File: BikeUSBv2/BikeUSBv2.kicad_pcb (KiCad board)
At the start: 2 copper layers, 43.6 x 25.2 mm, 48 parts, among them J1 TYPE-C-31-M-16, J2 Conn_01x02_Female, Q1 SSM3J332R,LF, Q2 SSM3J332R,LF, SW1 SW_Push, SW2 SW_Push, U1 TPS63020DSJR, U2 ATtiny1616-M

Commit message: actually complete routing
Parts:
- moved L1 0.30 mm to (149.5, 103.5)
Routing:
- net GND: vias 82 -> 111

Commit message: added pcb art, other stuff
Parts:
- added CAT**: PCBcat, H3_Other:PCBcat, B.Cu at (115.5, 102.2)
- added REF**: KiCad-Logo2_6mm_SilkScreen, Symbol:KiCad-Logo2_6mm_SilkScreen, B.Cu at (136.0, 91.0)
- L1: value 1u -> YPRH0704-1R0M
- moved L1 0.30 mm to (149.2, 103.5)
- moved SW1 0.20 mm to (112.7, 102.5)
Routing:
- net GND: vias 111 -> 113
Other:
- board text added: "BikeUSB by H3 v2.0"

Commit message: small stuff
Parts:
- added TP7: EN, TestPoint:TestPoint_Pad_D2.5mm, B.Cu at (129.4, 103.5)
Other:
- board text added: "@h3wastooshort /BikeUSBv2"

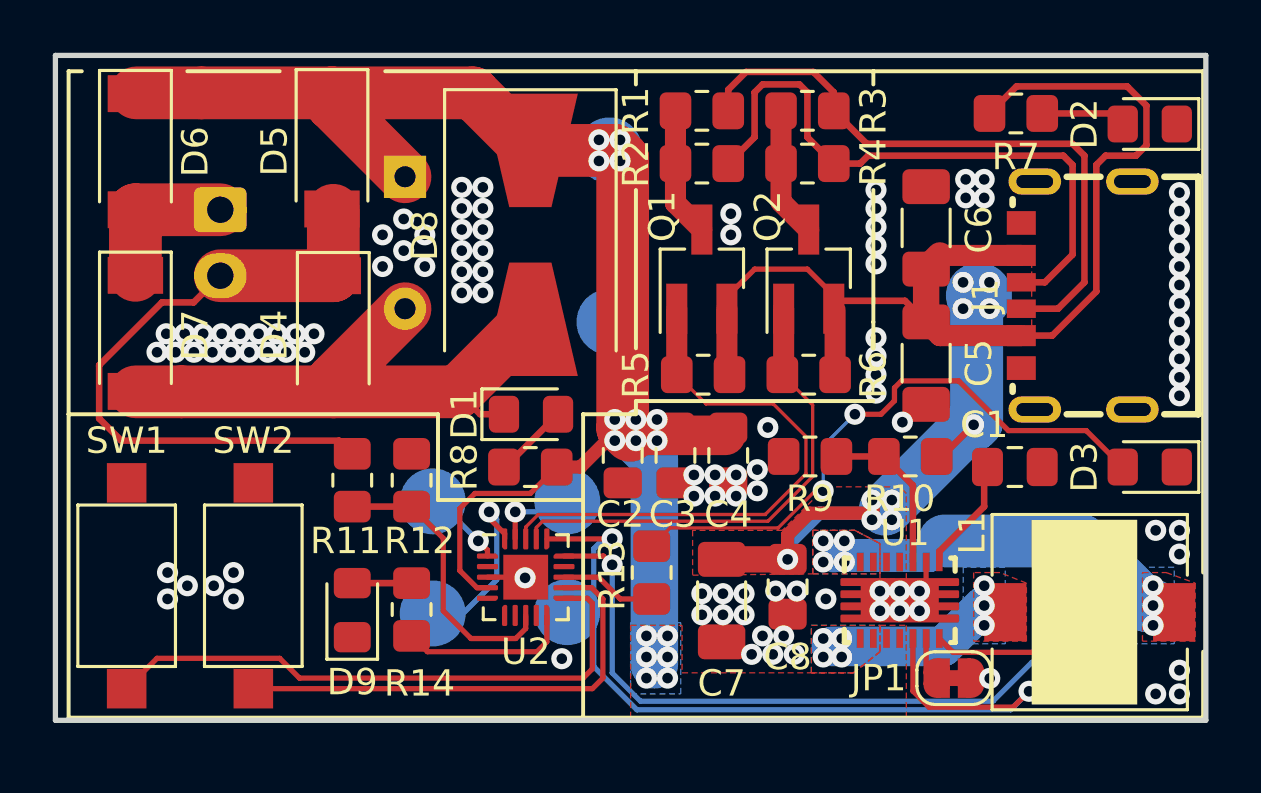
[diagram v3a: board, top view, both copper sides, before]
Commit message: better U1 cap layout
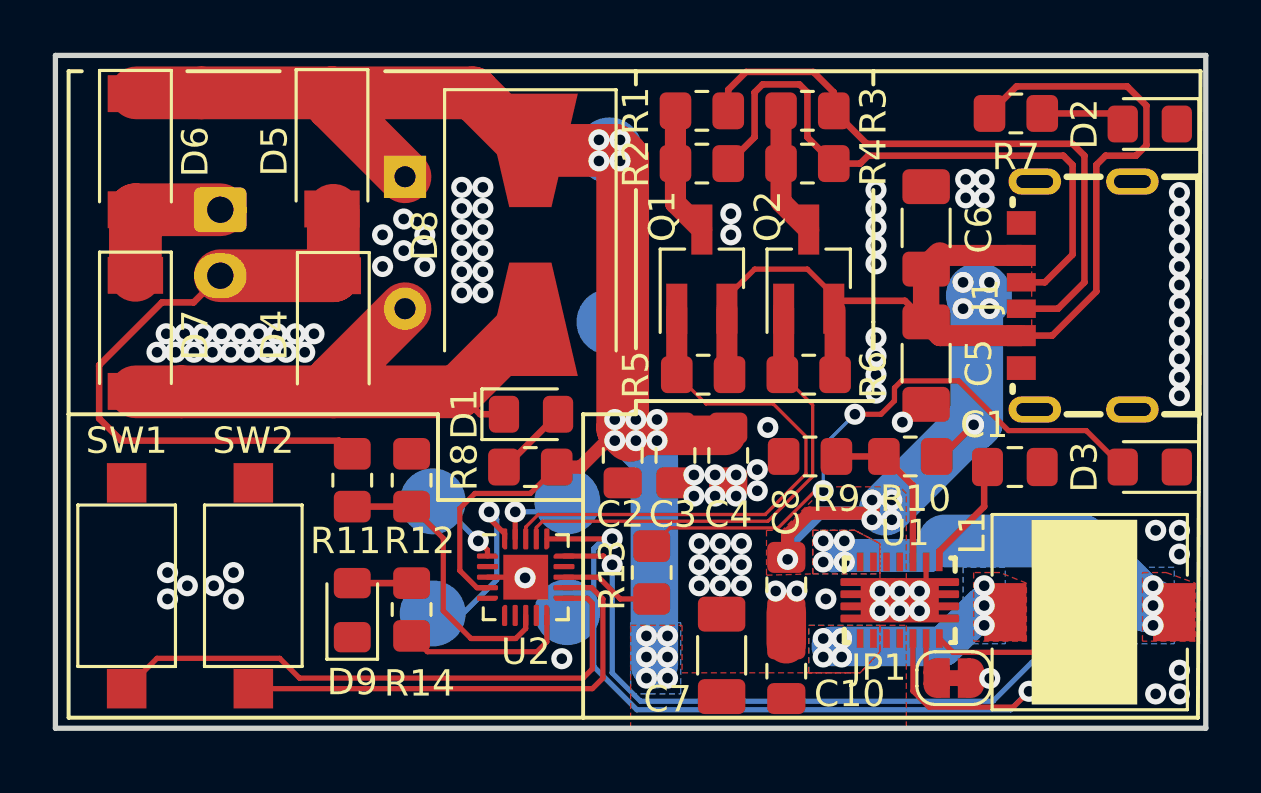
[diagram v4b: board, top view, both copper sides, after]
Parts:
- added C10: 100n, Capacitor_SMD:C_0805_2012Metric_Pad1.18x1.45mm_HandSolder, F.Cu at (137.7, 105.7)
- C2, C3: value 10u -> 4u7
- C4: value 100n -> 4u7
- moved C7 2.08 mm to (135.2, 105.1), turned to 90 degrees
- moved C8 0.09 mm to (137.7, 102.5)
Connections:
- C7 pad 1: +5V -> VCC
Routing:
- net +5V: track 66.2 -> 63.7 mm
- net GND: track 27.5 -> 28.7 mm, vias 113 -> 111
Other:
- board size 43.6 x 25.2 mm -> 43.6 x 25.5 mm

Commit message: cleanup
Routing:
- net GND: track 28.7 -> 26.1 mm
- net +5V: track 63.7 -> 62.0 mm
- net Net-(D2-A): track 3.22 -> 2.65 mm
- net Net-(U2-~{RESET}/PA0): track 3.16 -> 2.60 mm
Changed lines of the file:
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@@
     (property "ki_keywords" "cap capacitor")
     (attr smd)
-    (fp_text reference "C10" (at -0.8625 2.4 180) (layer "F.SilkS")
+    (fp_text reference "C10" (at -0.8625 2.4 270) (layer "F.SilkS")
         (effects (font (size 1 1) (thickness 0.15)))
     )
@@
     (attr exclude_from_pos_files allow_soldermask_bridges)
     (net_tie_pad_groups "1, 2")
-    (fp_text reference "JP1" (at 2.85 0.4 180) (layer "F.SilkS")
+    (fp_text reference "JP1" (at 2.25 -0.2 270) (layer "F.SilkS")
         (effects (font (size 1 1) (thickness 0.15)))
     )
@@
     (effects (font (size 1 1) (thickness 0.2) bold) (justify left bottom mirror))
   )
-  (segment (start 145.2 98.2) (end 145 98) (width 0.25) (layer "F.Cu") (net 1))
   (segment (start 143.5 101.6) (end 143.5 101.2) (width 0.25) (layer "F.Cu") (net 1))
   (segment (start 145.2 99.5) (end 145.2 98.2) (width 0.25) (layer "F.Cu") (net 1))
   (segment (start 143.5 101.2) (end 145.2 99.5) (width 0.25) (layer "F.Cu") (net 1))
-  (segment (start 143 102.6) (end 143 102.6) (width 0.2) (layer "F.Cu") (net 2))
-  (segment (start 141.75 103.35) (end 142.5 103.35) (width 0.2) (layer "F.Cu") (net 2))
   (segment (start 114.7825 95.15) (end 113.0475 95.15) (width 2) (layer "F.Cu") (net 2))
   (segment (start 120.5325 95.15) (end 114.7825 95.15) (width 2) (layer "F.Cu") (net 2))
-  (segment (start 142.5 102.6) (end 143 102.6) (width 0.2) (layer "F.Cu") (net 2))
   (segment (start 126.1 96) (end 125.25 95.15) (width 0.25) (layer "F.Cu") (net 2))
   (segment (start 120.5325 95.15) (end 120.5325 94.7175) (width 2) (layer "F.Cu") (net 2))
-  (segment (start 142.5 103.1) (end 142.5 102.6) (width 0.2) (layer "F.Cu") (net 2))
   (segment (start 120.5325 94.7175) (end 123.25 92) (width 2) (layer "F.Cu") (net 2))
-  (segment (start 142.5 103.35) (end 142.55 103.05) (width 0.2) (layer "F.Cu") (net 2))
-  (segment (start 142 103.05) (end 141.75 103.35) (width 0.2) (layer "F.Cu") (net 2))
   (segment (start 125.25 95.15) (end 128 92.4) (width 2) (layer "F.Cu") (net 2))
-  (segment (start 142.55 103.05) (end 142.5 103.1) (width 0.2) (layer "F.Cu") (net 2))
-  (segment (start 113.0475 95.15) (end 113.0325 95.135) (width 0.25) (layer "F.Cu") (net 2))
   (segment (start 143 102.6) (end 143 101.6) (width 0.2) (layer "F.Cu") (net 2))
   (segment (start 126.375 102.175) (end 127.825 102.175) (width 0.2) (layer "F.Cu") (net 2))
@@
   (segment (start 131.5 96.525) (end 131.775 96.8) (width 2) (layer "F.Cu") (net 3))
   (segment (start 120.4825 83.82) (end 120.4825 84.2325) (width 2) (layer "F.Cu") (net 3))
-  (segment (start 113.0625 83.82) (end 113.0325 83.85) (width 0.25) (layer "F.Cu") (net 3))
   (segment (start 120.4825 84.2325) (end 123.25 87) (width 2) (layer "F.Cu") (net 3))
-  (segment (start 115.5325 83.82) (end 113.0625 83.82) (width 2) (layer "F.Cu") (net 3))
   (segment (start 131.775 96.8) (end 135.4 96.8) (width 1.5) (layer "F.Cu") (net 3))
   (segment (start 129.9 98) (end 131.7 96.2) (width 0.5) (layer "F.Cu") (net 3))
   (segment (start 125.327 99.573) (end 125.9 99) (width 0.2) (layer "F.Cu") (net 3))
   (segment (start 125.975 102.575) (end 125.327 101.927) (width 0.2) (layer "F.Cu") (net 3))
-  (segment (start 120.4825 83.82) (end 115.5325 83.82) (width 2) (layer "F.Cu") (net 3))
+  (segment (start 113.0625 83.82) (end 120.4825 83.82) (width 2) (layer "F.Cu") (net 3))
   (segment (start 128 99) (end 129 98) (width 0.2) (layer "F.Cu") (net 3))
   (segment (start 125.327 101.927) (end 125.327 99.573) (width 0.2) (layer "F.Cu") (net 3))
@@
   (segment (start 138.5 90.5) (end 136.5 90.5) (width 0.2) (layer "F.Cu") (net 4))
   (segment (start 142.2 91.7) (end 143 92.5) (width 0.25) (layer "F.Cu") (net 4))
-  (segment (start 139.3 91.8) (end 139.3 91.3) (width 0.2) (layer "F.Cu") (net 4))
   (segment (start 143 92.5) (end 143 90.5) (width 1) (layer "F.Cu") (net 4))
   (segment (start 143.52 93.02) (end 146.6075 93.02) (width 0.8) (layer "F.Cu") (net 4))
   (segment (start 139.8 91.7) (end 142.2 91.7) (width 0.25) (layer "F.Cu") (net 4))
-  (segment (start 139.5 92) (end 139.3 91.8) (width 0.2) (layer "F.Cu") (net 4))
-  (segment (start 135.45 91.55) (end 135.45 92) (width 0.2) (layer "F.Cu") (net 4))
   (segment (start 143.52 89.98) (end 143 90.5) (width 1) (layer "F.Cu") (net 4))
   (segment (start 139.55 94.5) (end 139.55 92.05) (width 0.8) (layer "F.Cu") (net 4))
-  (segment (start 143.4 97.6) (end 143.6 97.6) (width 0.25) (layer "F.Cu") (net 4))
   (segment (start 138.574545 99.748417) (end 140.851583 99.748417) (width 0.5) (layer "F.Cu") (net 4))
   (segment (start 151.35 84.3049) (end 151.35 85.805) (width 0.25) (layer "F.Cu") (net 4))
@@
   (segment (start 137.75 100.572962) (end 138.574545 99.748417) (width 0.5) (layer "F.Cu") (net 4))
   (segment (start 147.78 93.02) (end 146.6075 93.02) (width 0.25) (layer "F.Cu") (net 4))
-  (segment (start 139.55 92.05) (end 139.5 92) (width 0.2) (layer "F.Cu") (net 4))
-  (segment (start 135.45 94.4) (end 135.55 94.5) (width 0.8) (layer "F.Cu") (net 4))
   (segment (start 146.6075 89.98) (end 143.52 89.98) (width 0.8) (layer "F.Cu") (net 4))
   (segment (start 150.955 86.2) (end 149.8 86.2) (width 0.25) (layer "F.Cu") (net 4))
@@
   (segment (start 137.75 101.5) (end 137.75 100.947918) (width 0.5) (layer "B.Cu") (net 4))
   (segment (start 144.9175 96.2825) (end 144.9175 91.5825) (width 2) (layer "B.Cu") (net 4))
-  (segment (start 144.9175 91.5825) (end 145 91.5) (width 2) (layer "B.Cu") (net 4))
   (segment (start 140.851583 99.748417) (end 141 99.6) (width 0.5) (layer "B.Cu") (net 4))
   (segment (start 138.949501 99.748417) (end 140.851583 99.748417) (width 0.5) (layer "B.Cu") (net 4))
@@
   (segment (start 141.45 99.6) (end 144.65 96.4) (width 2) (layer "B.Cu") (net 4))
   (segment (start 144.65 96.4) (end 144.8 96.4) (width 2) (layer "B.Cu") (net 4))
-  (segment (start 127 98) (end 127.05 98) (width 0.25) (layer "F.Cu") (net 5))
   (segment (start 127.05 98) (end 129.05 96) (width 0.25) (layer "F.Cu") (net 5))
   (segment (start 147.4 84.6) (end 150.05 84.6) (width 0.25) (layer "F.Cu") (net 6))
-  (segment (start 150.05 84.6) (end 150.45 85) (width 0.25) (layer "F.Cu") (net 6))
   (segment (start 142.0645 94.7355) (end 141.8 95) (width 0.2) (layer "F.Cu") (net 7))
   (segment (start 144.2355 94.7355) (end 142.0645 94.7355) (width 0.2) (layer "F.Cu") (net 7))
@@
   (segment (start 111.6575 96.16) (end 111.6575 94.1425) (width 0.25) (layer "F.Cu") (net 8))
   (segment (start 114.04 91.76) (end 115.24 91.76) (width 0.25) (layer "F.Cu") (net 8))
-  (segment (start 120.5325 88.27) (end 120.4825 88.22) (width 0.25) (layer "F.Cu") (net 8))
   (segment (start 120.5325 90.75) (end 120.5325 88.27) (width 2) (layer "F.Cu") (net 8))
   (segment (start 112.4975 97) (end 111.6575 96.16) (width 0.25) (layer "F.Cu") (net 8))
@@
   (segment (start 137.00521 100.054) (end 138.7 98.35921) (width 0.127) (layer "F.Cu") (net 18))
   (segment (start 128.464776 100.054) (end 137.00521 100.054) (width 0.127) (layer "F.Cu") (net 18))
-  (segment (start 137.6 94.45) (end 137.55 94.5) (width 0.2) (layer "F.Cu") (net 18))
   (segment (start 138.7 95.65) (end 137.55 94.5) (width 0.127) (layer "F.Cu") (net 18))
   (segment (start 137.5 87.95) (end 138.55 89) (width 0.8) (layer "F.Cu") (net 19))
@@
   (segment (start 127.425 99.701436) (end 127.425 100.725) (width 0.2) (layer "F.Cu") (net 24))
   (via (at 127.426936 99.6995) (size 0.8) (drill 0.4) (layers "F.Cu" "B.Cu") (net 24))
-  (segment (start 129.0005 99.6995) (end 129.4 99.3) (width 0.2) (layer "B.Cu") (net 24))
   (segment (start 127.426936 99.6995) (end 129.0005 99.6995) (width 0.2) (layer "B.Cu") (net 24))
   (segment (start 126.438193 99.938193) (end 127.025 100.525) (width 0.2) (layer "F.Cu") (net 25))
   (segment (start 126.438193 99.6995) (end 126.438193 99.938193) (width 0.2) (layer "F.Cu") (net 25))
-  (segment (start 127.025 100.525) (end 127.025 100.725) (width 0.2) (layer "F.Cu") (net 25))
   (via (at 126.438193 99.6995) (size 0.8) (drill 0.4) (layers "F.Cu" "B.Cu") (net 25))
   (segment (start 126.7265 99.987807) (end 126.7265 102.2735) (width 0.2) (layer "B.Cu") (net 25))
@@
   (segment (start 126.0265 100.8) (end 126.375 101.1485) (width 0.2) (layer "F.Cu") (net 26))
   (via (at 126.0265 100.8) (size 0.8) (drill 0.4) (layers "F.Cu" "B.Cu") (net 26))
-  (segment (start 124.5265 99.3) (end 124.3 99.3) (width 0.2) (layer "B.Cu") (net 26))
   (segment (start 126.0265 100.8) (end 124.5265 99.3) (width 0.2) (layer "B.Cu") (net 26))
   (segment (start 128.625 100.725) (end 131.0925 100.725) (width 0.2) (layer "F.Cu") (net 27))
@@
   (segment (start 130.75 106) (end 130.75 103) (width 0.2) (layer "F.Cu") (net 34))
   (segment (start 130.75 103) (end 130.32088 102.57088) (width 0.2) (layer "F.Cu") (net 34))
-  (segment (start 129.27912 102.57088) (end 129.275 102.575) (width 0.19) (layer "F.Cu") (net 34))
   (segment (start 130.35 106.4) (end 130.75 106) (width 0.2) (layer "F.Cu") (net 34))
   (segment (start 117.5 106.4) (end 130.35 106.4) (width 0.2) (layer "F.Cu") (net 34))

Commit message: switch diode footprints
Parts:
- D4, D5, D6, D7: footprint Diode_SMD:D_SOD-128 -> Diode_SMD:D_PowerDI-123
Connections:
- R11 pad 2: /AC1 -> /AC2
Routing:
- net /AC1: track 24.9 -> 6.76 mm
- net /AC2: track 5.70 -> 20.6 mm
- net VCC: track 58.6 -> 57.4 mm
- net GND: track 26.1 -> 25.0 mm, vias 111 -> 106
